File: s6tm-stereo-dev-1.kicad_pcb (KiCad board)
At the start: 4 copper layers, 191 parts, among them J1 Micro_SD_Card_Det1, J2 Conn_01x04_Pin, J3 USB_C_Receptacle_USB2.0_14P, J4 Conn_01x02, J5 AudioJack4, J6 Conn_01x02, J7 Conn_01x02, J8 Conn_01x02, Q1 Q_NMOS, Q2 Q_NMOS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

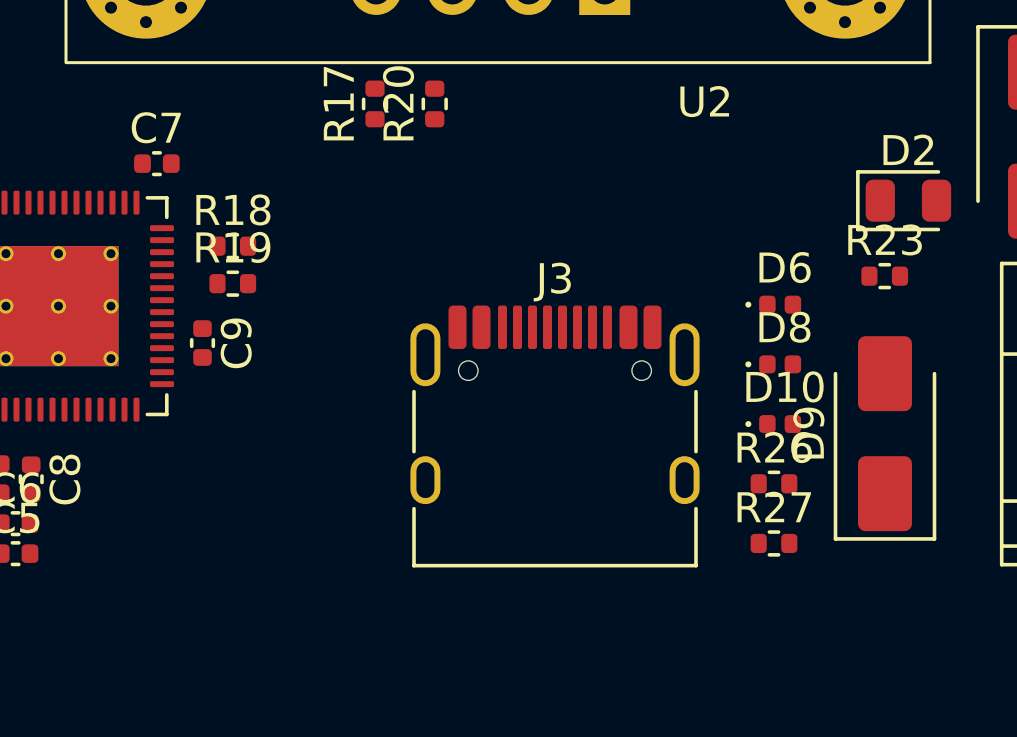
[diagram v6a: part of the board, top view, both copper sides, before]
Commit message: pcb: add usb layout
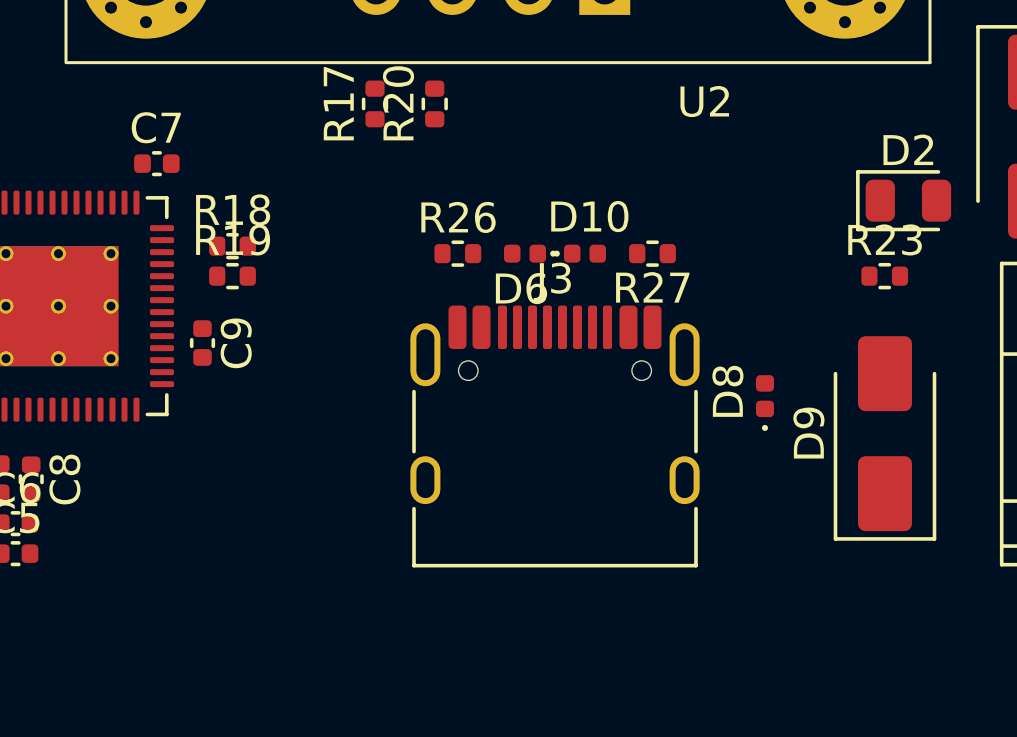
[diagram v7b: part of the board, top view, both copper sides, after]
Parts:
- moved R26 13.0 mm to (81.8, 177.0)
- moved R27 10.5 mm to (88.2, 177.0), turned to 180 degrees
- moved D6 8.67 mm to (84.0, 177.0), turned to 180 degrees
- moved D10 8.64 mm to (86.0, 177.0)
- moved D8 1.17 mm to (92.0, 181.8), turned to 90 degrees
- moved R19 0.25 mm to (74.2, 177.8)
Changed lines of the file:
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@@
 	(footprint "GLCS:Diode_DFN1006"
 		(layer "F.Cu")
-		(at 92.505 178.7)
+		(at 84 177 180)
 		(descr "Diode SMD 0402 (1005 Metric), square (rectangular) end terminal, IPC-7351 nominal, (Body size source: http://www.tortai-tech.com/upload/download/2011102023233369053.pdf), generated with kicad-footprint-generator")
 		(tags "diode")
@@
 		)
 		(property "Basic" "E"
-			(at 0 0 0)
+			(at 0 0 180)
 			(unlocked yes)
 			(layer "F.Fab")
@@
 		)
 		(property "JLCPCB Part #" "C22395519"
-			(at 0 0 0)
+			(at 0 0 180)
 			(unlocked yes)
 			(layer "F.Fab")
@@
 		)
 		(property "Manufacturer" "hongjiacheng"
-			(at 0 0 0)
+			(at 0 0 180)
 			(unlocked yes)
 			(layer "F.Fab")
@@
 		)
 		(property "Manufacturer Part Number" "H5VU10U"
-			(at 0 0 0)
+			(at 0 0 180)
 			(unlocked yes)
 			(layer "F.Fab")
@@
 		)
 		(fp_line
-			(start -0.86 -0.47)
-			(end 0.87 -0.47)
+			(start 0.87 0.47)
+			(end -0.86 0.47)
 			(stroke
 				(width 0.05)
@@
 		)
 		(fp_line
-			(start -0.86 0.47)
-			(end -0.86 -0.47)
+			(start 0.87 -0.47)
+			(end 0.87 0.47)
 			(stroke
 				(width 0.05)
@@
 		)
 		(fp_line
-			(start 0.87 -0.47)
-			(end 0.87 0.47)
+			(start -0.86 0.47)
+			(end -0.86 -0.47)
 			(stroke
 				(width 0.05)
@@
 		)
 		(fp_line
-			(start 0.87 0.47)
-			(end -0.86 0.47)
+			(start -0.86 -0.47)
+			(end 0.87 -0.47)
 			(stroke
 				(width 0.05)
@@
 		)
 		(fp_line
-			(start -0.56 -0.25)
-			(end 0.44 -0.25)
+			(start 0.44 0.25)
+			(end -0.56 0.25)
 			(stroke
 				(width 0.1)
@@
 		)
 		(fp_line
-			(start -0.56 0.25)
-			(end -0.56 -0.25)
+			(start 0.44 -0.25)
+			(end 0.44 0.25)
 			(stroke
 				(width 0.1)
@@
 		)
 		(fp_line
-			(start -0.46 0.25)
-			(end -0.46 -0.25)
+			(start -0.36 0.25)
+			(end -0.36 -0.25)
 			(stroke
 				(width 0.1)
@@
 		)
 		(fp_line
-			(start -0.36 0.25)
-			(end -0.36 -0.25)
+			(start -0.46 0.25)
+			(end -0.46 -0.25)
 			(stroke
 				(width 0.1)
@@
 		)
 		(fp_line
-			(start 0.44 -0.25)
-			(end 0.44 0.25)
+			(start -0.56 0.25)
+			(end -0.56 -0.25)
 			(stroke
 				(width 0.1)
@@
 		)
 		(fp_line
-			(start 0.44 0.25)
-			(end -0.56 0.25)
+			(start -0.56 -0.25)
+			(end 0.44 -0.25)
 			(stroke
 				(width 0.1)
@@
 		)
 		(pad "1" smd roundrect
-			(at -0.425 0)
+			(at -0.425 0 180)
 			(size 0.55 0.6)
 			(layers "F.Cu" "F.Mask" "F.Paste")
@@
 		)
 		(pad "2" smd roundrect
-			(at 0.425 0)
+			(at 0.425 0 180)
 			(size 0.55 0.6)
 			(layers "F.Cu" "F.Mask" "F.Paste")
@@
 	(footprint "GLCS:Diode_DFN1006"
 		(layer "F.Cu")
-		(at 92.505 182.68)
+		(at 86 177)
 		(descr "Diode SMD 0402 (1005 Metric), square (rectangular) end terminal, IPC-7351 nominal, (Body size source: http://www.tortai-tech.com/upload/download/2011102023233369053.pdf), generated with kicad-footprint-generator")
 		(tags "diode")
@@
 	(footprint "Resistor_SMD:R_0402_1005Metric"
 		(layer "F.Cu")
-		(at 74.26 178)
+		(at 74.25 177.75)
 		(descr "Resistor SMD 0402 (1005 Metric), square (rectangular) end terminal, IPC-7351 nominal, (Body size source: IPC-SM-782 page 72, https://www.pcb-3d.com/wordpress/wp-content/uploads/ipc-sm-782a_amendment_1_and_2.pdf)")
 		(tags "resistor")
@@
 	(footprint "Resistor_SMD:R_0402_1005Metric"
 		(layer "F.Cu")
-		(at 92.3 184.67)
+		(at 81.76 177)
 		(descr "Resistor SMD 0402 (1005 Metric), square (rectangular) end terminal, IPC-7351 nominal, (Body size source: IPC-SM-782 page 72, https://www.pcb-3d.com/wordpress/wp-content/uploads/ipc-sm-782a_amendment_1_and_2.pdf)")
 		(tags "resistor")
@@
 	(footprint "GLCS:Diode_DFN1006"
 		(layer "F.Cu")
-		(at 92.505 180.69)
+		(at 92 181.75 90)
 		(descr "Diode SMD 0402 (1005 Metric), square (rectangular) end terminal, IPC-7351 nominal, (Body size source: http://www.tortai-tech.com/upload/download/2011102023233369053.pdf), generated with kicad-footprint-generator")
 		(tags "diode")
 		(property "Reference" "D8"
-			(at 0.14 -1.2 0)
+			(at 0.14 -1.2 90)
 			(layer "F.SilkS")
 			(effects
@@
 		)
 		(property "Value" "H5VU10U"
-			(at -0.06 1.17 0)
+			(at -0.06 1.17 90)
 			(layer "F.Fab")
 			(effects
@@
 		)
 		(property "Datasheet" "https://datasheet.lcsc.com/lcsc/2504101957_hongjiacheng-H5VU10U_C22395519.pdf"
-			(at 0 0 0)
+			(at 0 0 90)
 			(layer "F.Fab")
 			(hide yes)
@@
 		)
 		(property "Description" "-55℃~+155℃ 0.8pF 16V 200nA 55W@8/20us 5A@8/20us 5V 6V ESD IEC 61000-4-2 Unidirectional DFN1006-2L ESD and Surge Protection (TVS/ESD) ROHS"
-			(at 0 0 0)
+			(at 0 0 90)
 			(layer "F.Fab")
 			(hide yes)
@@
 		)
 		(property "Basic" "E"
-			(at 0 0 0)
+			(at 0 0 90)
 			(unlocked yes)
 			(layer "F.Fab")
@@
 		)
 		(property "JLCPCB Part #" "C22395519"
-			(at 0 0 0)
+			(at 0 0 90)
 			(unlocked yes)
 			(layer "F.Fab")
@@
 		)
 		(property "Manufacturer" "hongjiacheng"
-			(at 0 0 0)
+			(at 0 0 90)
 			(unlocked yes)
 			(layer "F.Fab")
@@
 		)
 		(property "Manufacturer Part Number" "H5VU10U"
-			(at 0 0 0)
+			(at 0 0 90)
 			(unlocked yes)
 			(layer "F.Fab")
@@
 		)
 		(fp_line
-			(start -0.86 -0.47)
-			(end 0.87 -0.47)
+			(start 0.87 -0.47)
+			(end 0.87 0.47)
 			(stroke
 				(width 0.05)
@@
 		)
 		(fp_line
-			(start -0.86 0.47)
-			(end -0.86 -0.47)
+			(start -0.86 -0.47)
+			(end 0.87 -0.47)
 			(stroke
 				(width 0.05)
@@
 		)
 		(fp_line
-			(start 0.87 -0.47)
-			(end 0.87 0.47)
+			(start 0.87 0.47)
+			(end -0.86 0.47)
 			(stroke
 				(width 0.05)
@@
 		)
 		(fp_line
-			(start 0.87 0.47)
-			(end -0.86 0.47)
+			(start -0.86 0.47)
+			(end -0.86 -0.47)
 			(stroke
 				(width 0.05)
@@
 		)
 		(fp_line
-			(start -0.56 -0.25)
-			(end 0.44 -0.25)
+			(start 0.44 -0.25)
+			(end 0.44 0.25)
 			(stroke
 				(width 0.1)
@@
 		)
 		(fp_line
-			(start -0.56 0.25)
-			(end -0.56 -0.25)
+			(start -0.56 -0.25)
+			(end 0.44 -0.25)
 			(stroke
 				(width 0.1)
@@
 		)
 		(fp_line
-			(start -0.46 0.25)
-			(end -0.46 -0.25)
+			(start 0.44 0.25)
+			(end -0.56 0.25)
 			(stroke
 				(width 0.1)
@@
 		)
 		(fp_line
-			(start 0.44 -0.25)
-			(end 0.44 0.25)
+			(start -0.46 0.25)
+			(end -0.46 -0.25)
 			(stroke
 				(width 0.1)
@@
 		)
 		(fp_line
-			(start 0.44 0.25)
-			(end -0.56 0.25)
+			(start -0.56 0.25)
+			(end -0.56 -0.25)
 			(stroke
 				(width 0.1)
@@
 		)
 		(fp_text user "${REFERENCE}"
-			(at -0.06 0 0)
+			(at -0.06 0 90)
 			(layer "F.Fab")
 			(effects
@@
 		)
 		(pad "1" smd roundrect
-			(at -0.425 0)
+			(at -0.425 0 90)
 			(size 0.55 0.6)
 			(layers "F.Cu" "F.Mask" "F.Paste")
@@
 		)
 		(pad "2" smd roundrect
-			(at 0.425 0)
+			(at 0.425 0 90)
 			(size 0.55 0.6)
 			(layers "F.Cu" "F.Mask" "F.Paste")
@@
 	(footprint "Resistor_SMD:R_0402_1005Metric"
 		(layer "F.Cu")
-		(at 92.3 186.66)
+		(at 88.25 177 180)
 		(descr "Resistor SMD 0402 (1005 Metric), square (rectangular) end terminal, IPC-7351 nominal, (Body size source: IPC-SM-782 page 72, https://www.pcb-3d.com/wordpress/wp-content/uploads/ipc-sm-782a_amendment_1_and_2.pdf)")
 		(tags "resistor")
@@
 		)
 		(property "Manufacturer" "Uniroyal Elec"
-			(at 0 0 0)
+			(at 0 0 180)
 			(unlocked yes)
 			(layer "F.Fab")
@@
 		)
 		(property "Manufacturer Part Number" "0402WGF5101TCE"
-			(at 0 0 0)
+			(at 0 0 180)
 			(unlocked yes)
 			(layer "F.Fab")
@@
 		)
 		(property "Basic" "Y"
-			(at 0 0 0)
+			(at 0 0 180)
 			(unlocked yes)
 			(layer "F.Fab")
@@
 		)
 		(property "JLCPCB Part #" "C25905"
-			(at 0 0 0)
+			(at 0 0 180)
 			(unlocked yes)
 			(layer "F.Fab")
@@
 		(duplicate_pad_numbers_are_jumpers no)
 		(fp_line
-			(start -0.153641 -0.38)
-			(end 0.153641 -0.38)
+			(start -0.153641 0.38)
+			(end 0.153641 0.38)
 			(stroke
 				(width 0.12)
@@
 		)
 		(fp_line
-			(start -0.153641 0.38)
-			(end 0.153641 0.38)
+			(start -0.153641 -0.38)
+			(end 0.153641 -0.38)
 			(stroke
 				(width 0.12)
@@
 		)
 		(pad "1" smd roundrect
-			(at -0.51 0)
+			(at -0.51 0 180)
 			(size 0.54 0.64)
 			(layers "F.Cu" "F.Mask" "F.Paste")
@@
 		)
 		(pad "2" smd roundrect
-			(at 0.51 0)
+			(at 0.51 0 180)
 			(size 0.54 0.64)
 			(layers "F.Cu" "F.Mask" "F.Paste")
@@
 	(footprint "Resistor_SMD:R_0402_1005Metric"
 		(layer "F.Cu")
-		(at 74.26 176.75)
+		(at 74.25 176.75)
 		(descr "Resistor SMD 0402 (1005 Metric), square (rectangular) end terminal, IPC-7351 nominal, (Body size source: IPC-SM-782 page 72, https://www.pcb-3d.com/wordpress/wp-content/uploads/ipc-sm-782a_amendment_1_and_2.pdf)")
 		(tags "resistor")

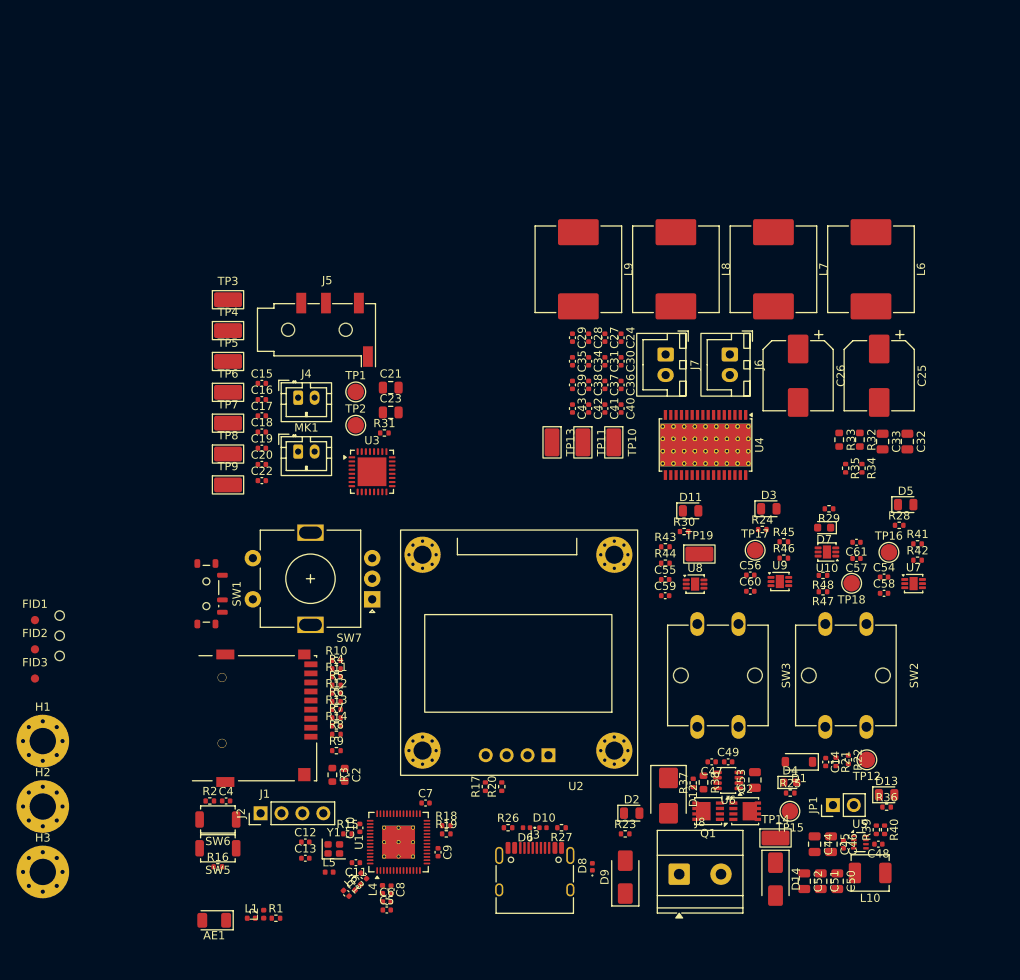
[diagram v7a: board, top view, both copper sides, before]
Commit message: pcb: add LDOs layout
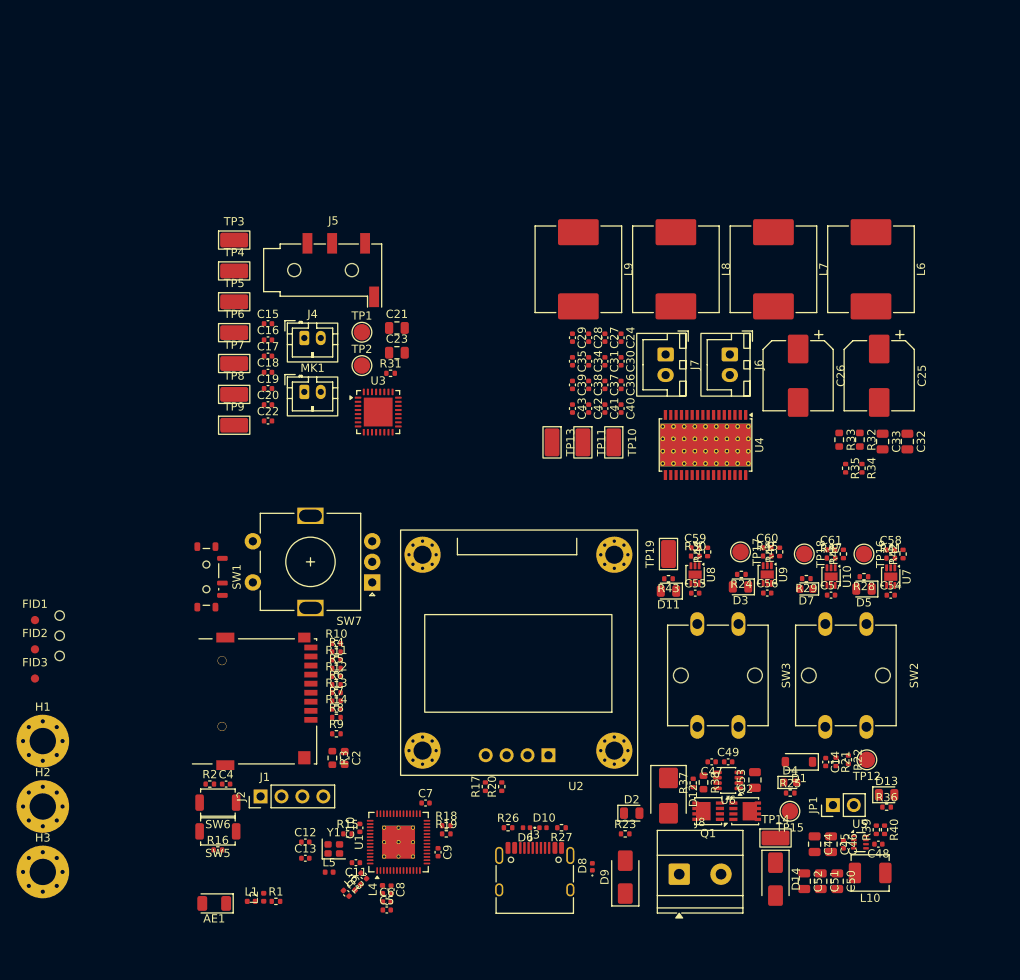
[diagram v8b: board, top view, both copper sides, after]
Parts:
- moved D5 11.4 mm to (125.0, 148.0), turned to 180 degrees
- moved D11 10.1 mm to (101.2, 148.2), turned to 180 degrees
- moved D3 10.1 mm to (110.0, 147.7), turned to 180 degrees
- moved R29 8.92 mm to (118.0, 146.7)
- moved D7 7.76 mm to (118.0, 148.0)
- moved R28 7.57 mm to (125.0, 146.5), turned to 180 degrees
- moved C20 7.29 mm to (52.6, 125.6)
- moved C22 7.29 mm to (52.6, 127.6)
- moved MK1 7.29 mm to (57.0, 124.0)
- moved C15 7.29 mm to (52.6, 115.8)
- moved C16 7.29 mm to (52.6, 117.7)
- moved C17 7.29 mm to (52.6, 119.7)
- moved C21 7.29 mm to (68.2, 116.3)
- moved C23 7.29 mm to (68.2, 119.3)
- moved J4 7.29 mm to (57.0, 117.5)
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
